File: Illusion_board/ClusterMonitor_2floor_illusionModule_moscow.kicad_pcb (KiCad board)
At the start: 2 copper layers, 278.6 x 113.3 mm, 109 parts, among them J1 RJ45_Molex_smd_44144-0003, J2 Conn_01x07, SW1 SW_SPST_Double, SW2 ADDRESS_SELECT, SW3 SW_SPDT, U1 AMS1117-3.3, U2 STM32F030C8Tx

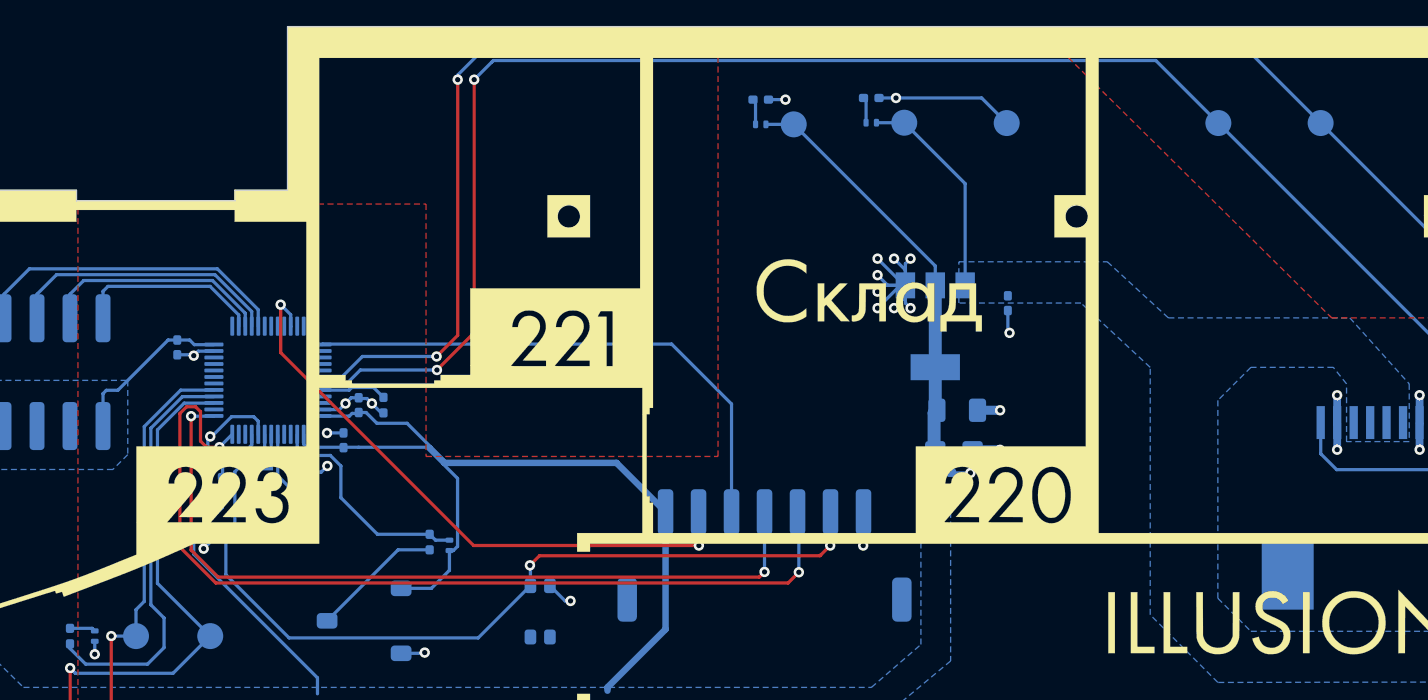
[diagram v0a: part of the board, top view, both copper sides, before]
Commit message: Some changes
Add stencil board layout.
Add gerbers.
Minor changes in expancion and atrium board.
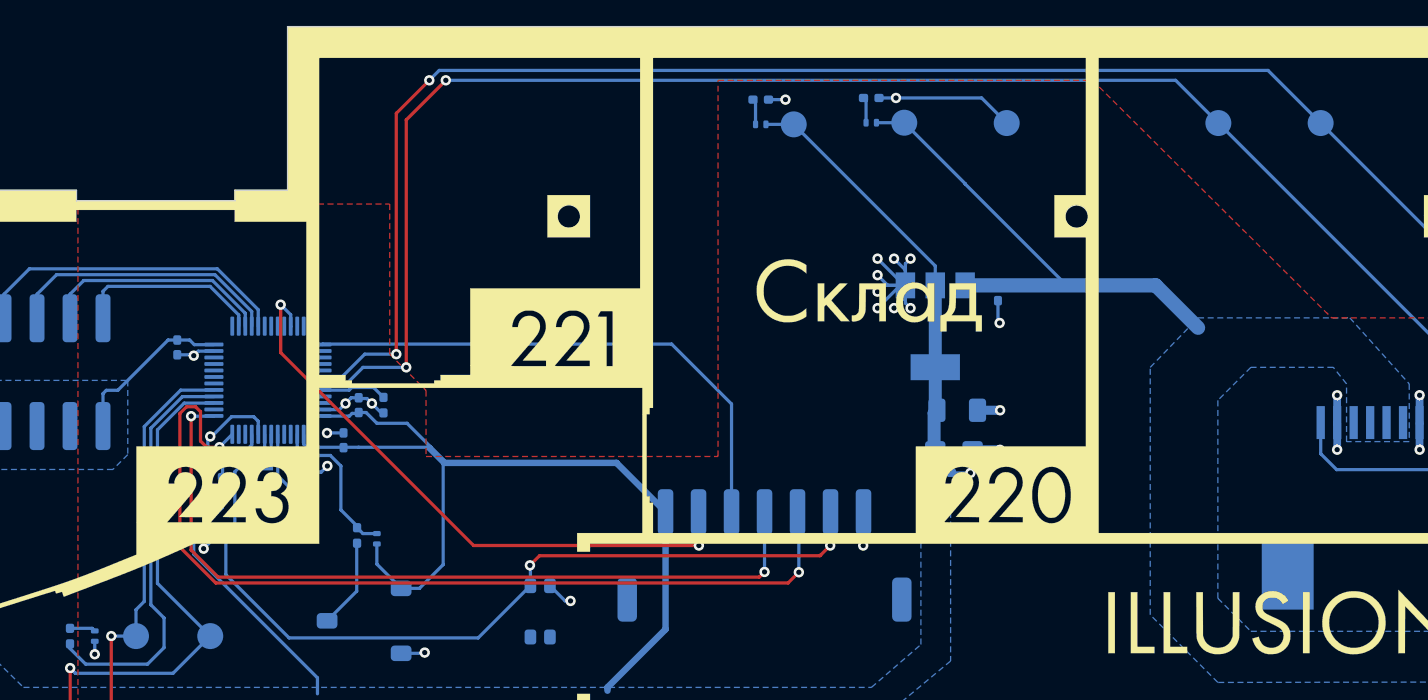
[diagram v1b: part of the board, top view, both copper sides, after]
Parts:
- moved D4 5.61 mm to (-201.9, 131.3)
- moved R5 5.61 mm to (-203.4, 131.1)
- moved C2 1.08 mm to (-154.1, 112.4)
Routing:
- net +5V: track 77.8 -> 99.9 mm
- net SWITCH_MODE: track 17.1 -> 11.7 mm
- net Net-(R5-Pad2): track 10.2 -> 7.00 mm
- net VDDA: track 147.0 -> 149.5 mm
- net I2C2_SCL: track 145.3 -> 143.4 mm
- net I2C2_SDA: track 122.7 -> 121.2 mm
